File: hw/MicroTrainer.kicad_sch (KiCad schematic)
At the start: 68 parts, among them J1 Conn_ARM_SWD_TagConnect_TC2030, J4 Conn_01x04, J5 Conn_01x08, J6 USB_C_Receptacle_USB2.0, SW1 KEY_C, SW10 KEY_B, SW11 KEY_ADDR, SW13 KEY_4, SW14 KEY_5, SW15 KEY_6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

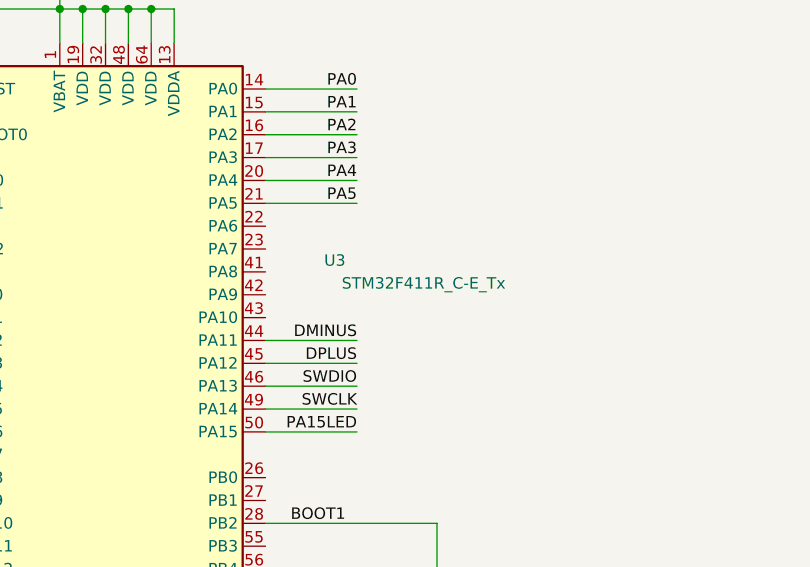
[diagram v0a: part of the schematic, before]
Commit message: Update to reflect we're using STM32F412
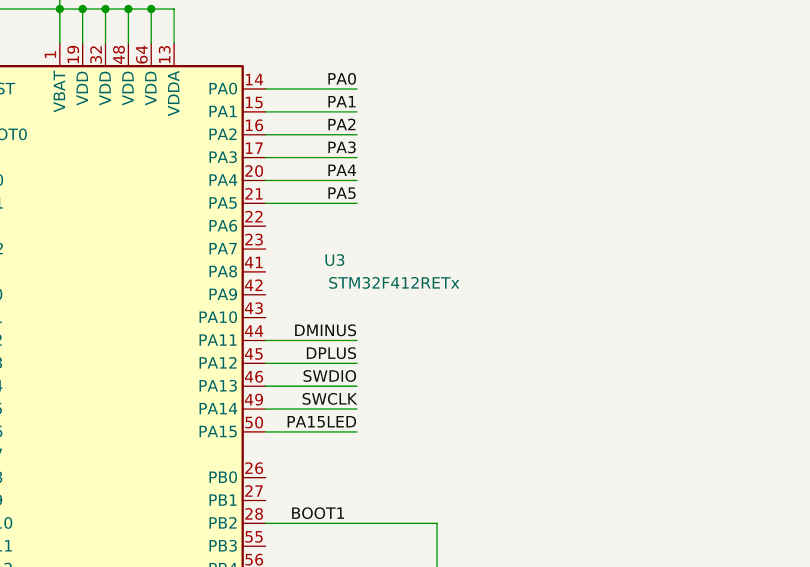
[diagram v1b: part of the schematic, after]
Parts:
- U3: value STM32F411R_C-E_Tx -> STM32F412RETx
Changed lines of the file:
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@@
       (effects (font (size 1.27 1.27)) (justify right))
     )
-    (property "Value" "STM32F411R_C-E_Tx" (at 121.92 52.07 0)
+    (property "Value" "STM32F412RETx" (at 116.84 52.07 0)
       (effects (font (size 1.27 1.27)) (justify right))
     )
